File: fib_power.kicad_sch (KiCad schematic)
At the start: 0 parts

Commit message: added several ICs, implementted schematics for charger, boost converter and LDOs
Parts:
- added C21, C28, C29, C31, C32: 10uF, symbol Device:C_Small
- added C22, C23, C25, C26, C27: 22uF, symbol Device:C_Small
- added C24: 330uF, symbol Device:C_Polarized_Small
- added C30, C33: 0.1uF, symbol Device:C_Small
- added L2: 1uH, symbol Device:L_Small
- added R11, R12: 100K, symbol Device:R_Small
- added U2: TPS61022RWUR, Fibel2:TPS61022RWUR, symbol Fibel2:TPS61022RWUR
- added U5: TLV75718PDBV, Package_TO_SOT_SMD:SOT-23-5, symbol Regulator_Linear:TLV75718PDBV
- added U6: TLV75733PDBV, Package_TO_SOT_SMD:SOT-23-5, symbol Regulator_Linear:TLV75733PDBV
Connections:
- new net: L2.2, U2.2 (SW)
- new net: R12.1, U2.4 (FB)
- new net: C22.2, C23.2, C24.2, C25.2
- new net +1V8: C28.1, C29.1, C30.1, U5.5 (OUT)
- new net +3V3: C31.1, C32.1, C33.1, U6.5 (OUT)
- new net +5V: C22.1, C23.1, C24.1, C25.1, C26.1, C27.1, R11.2, R12.2, U2.3 (VOUT), U5.1 (IN), U6.1 (IN)
- new net 5V_EN: U2.5 (EN)
- new net CARRIER_EN: U5.3 (EN), U6.3 (EN)
- new net GND: C21.2, C26.2, C27.2, C28.2, C29.2, C30.2, C31.2, C32.2, C33.2, R11.1, U2.1 (GND), U5.2 (GND), U6.2 (GND)
- new net VCC: C21.1, L2.1, U2.6 (MODE), U2.7 (VIN)
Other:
- note added: "RTC"
- note added: "SEQUENCING"

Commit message: added symbol&footprint for orin/sodimm, added a bunch of specs and docs, partially implemented audio, full steam ahead
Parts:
- C21, C28, C29, C30, C31, C32, C33: footprint (none) -> Capacitor_SMD:C_0603_1608Metric
- C22, C23, C25, C26, C27: footprint (none) -> Capacitor_SMD:C_0805_2012Metric
- C24: footprint (none) -> Capacitor_Tantalum_SMD:CP_EIA-6032-15_Kemet-U
- R11, R12: footprint (none) -> Resistor_SMD:R_0603_1608Metric

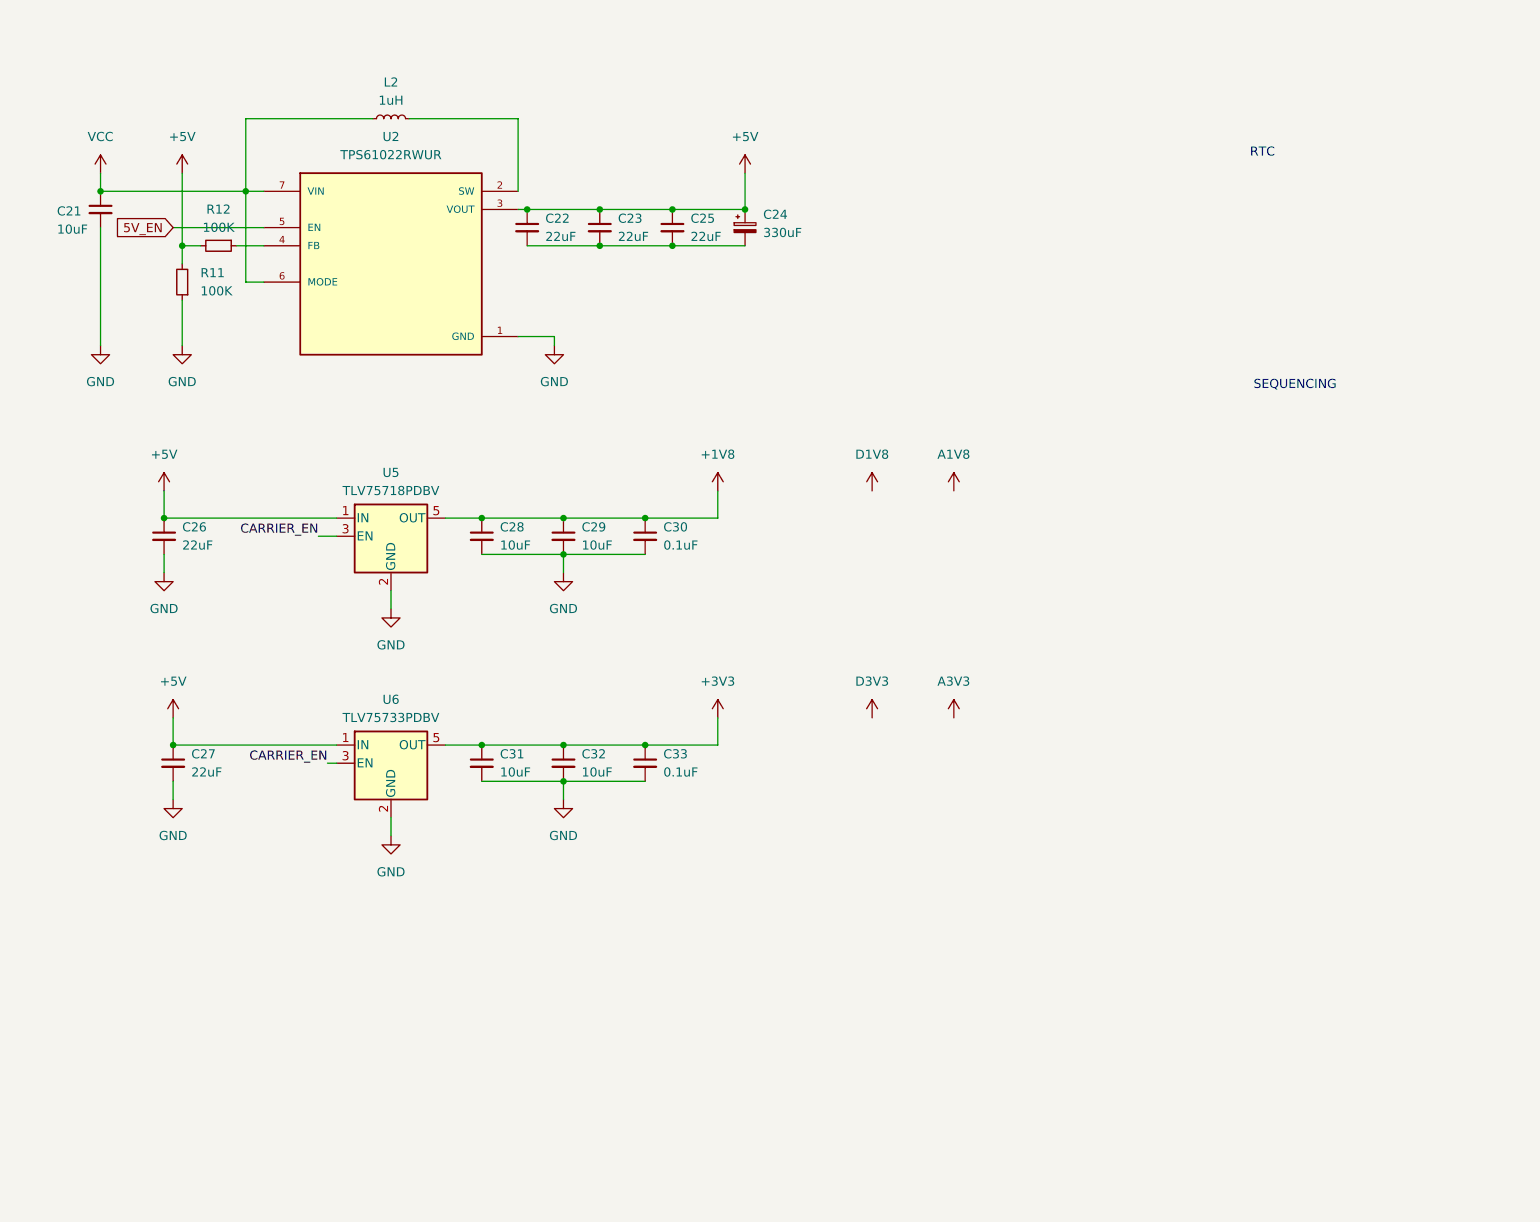
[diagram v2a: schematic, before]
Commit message: added usb+PD+DP & pcie implementations from antmicro design, added specs for USB components, rethought power+usb arch
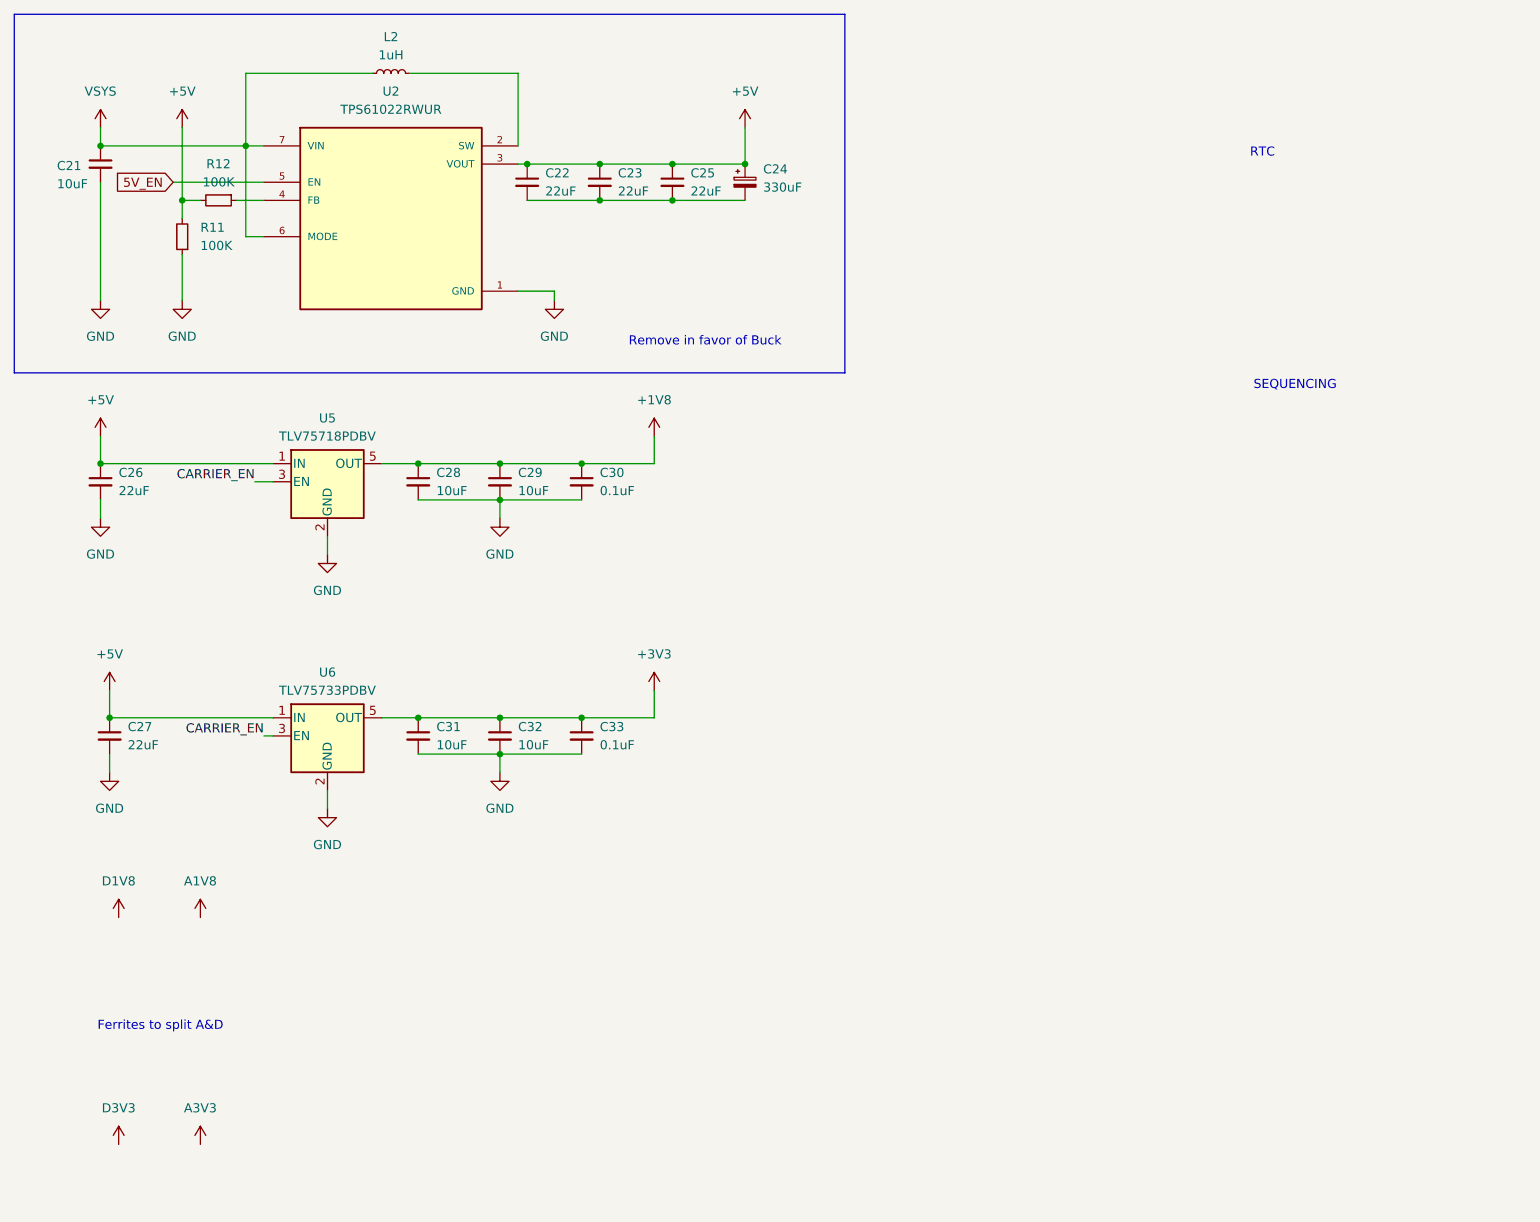
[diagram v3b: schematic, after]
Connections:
- net VCC renamed VSYS
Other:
- note added: "Ferrites to split A&D"
- note added: "Remove in favor of Buck"
- moved on the sheet: C21, C22, C23, C24, C25, C26, C27, C28, C29, C30, C31, C32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

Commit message: added nets for 40 pin headers (epd & rpi header) connected some of the nets i'm reeusing
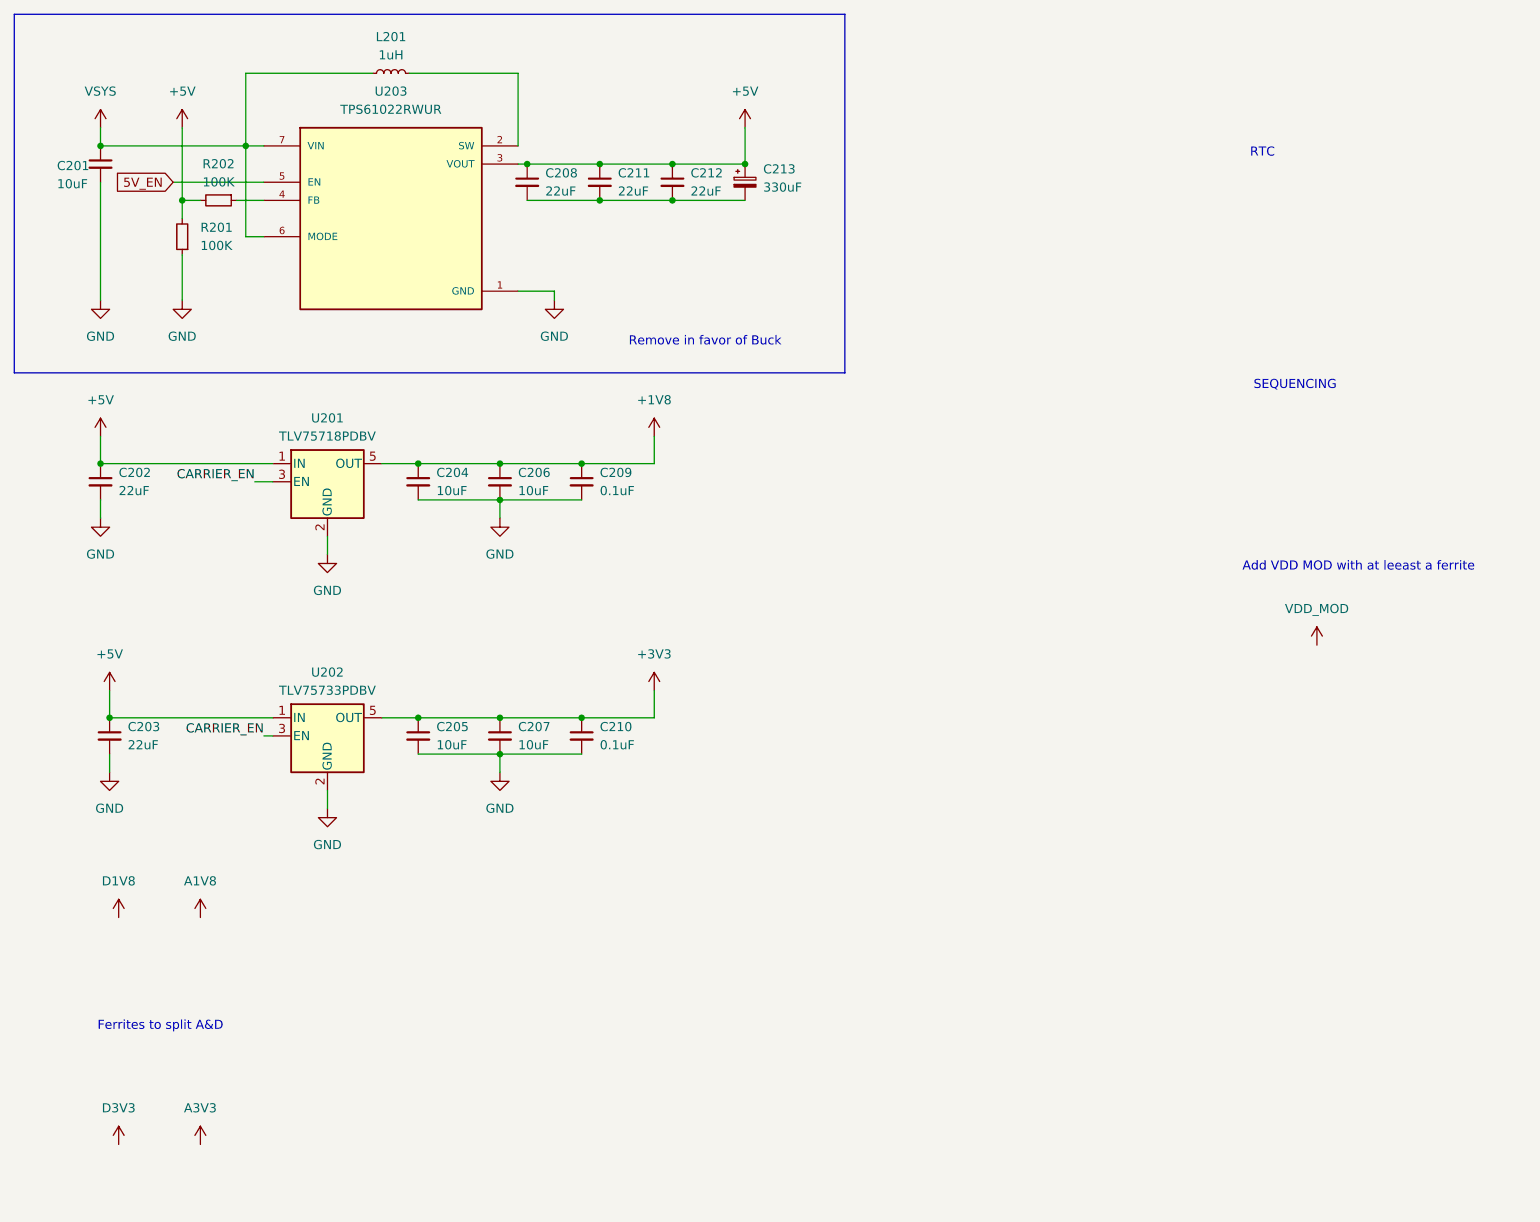
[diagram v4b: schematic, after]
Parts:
- renumbered C21 to C201, C26 to C202, C27 to C203, C28 to C204, C31 to C205, C29 to C206, C32 to C207, C22 to C208, C30 to C209, C33 to C210, C23 to C211, C25 to C212, C24 to C213, L2 to L201, R11 to R201, R12 to R202, U5 to U201, U6 to U202, U2 to U203
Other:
- note added: "Add VDD MOD with at leeast a ferrite"

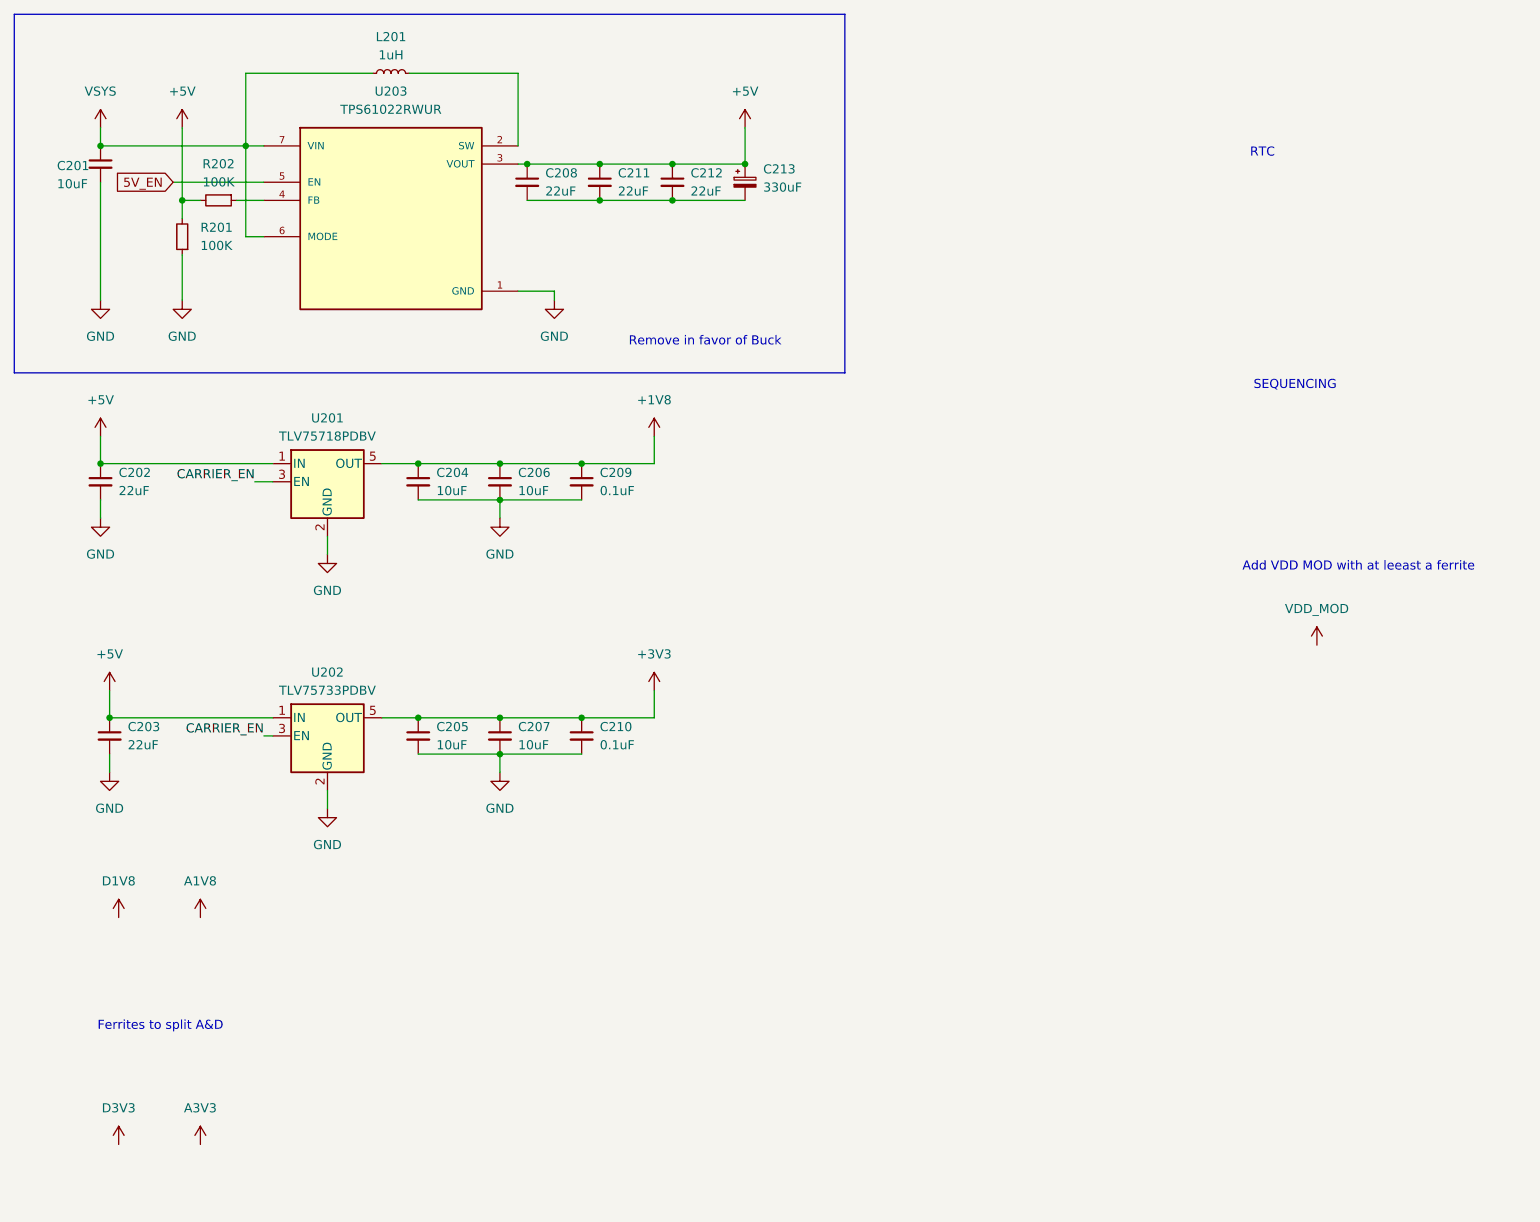
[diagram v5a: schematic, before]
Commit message: added buck converter, refactoored peripherals and updated gpio/SPI/i2c mapping
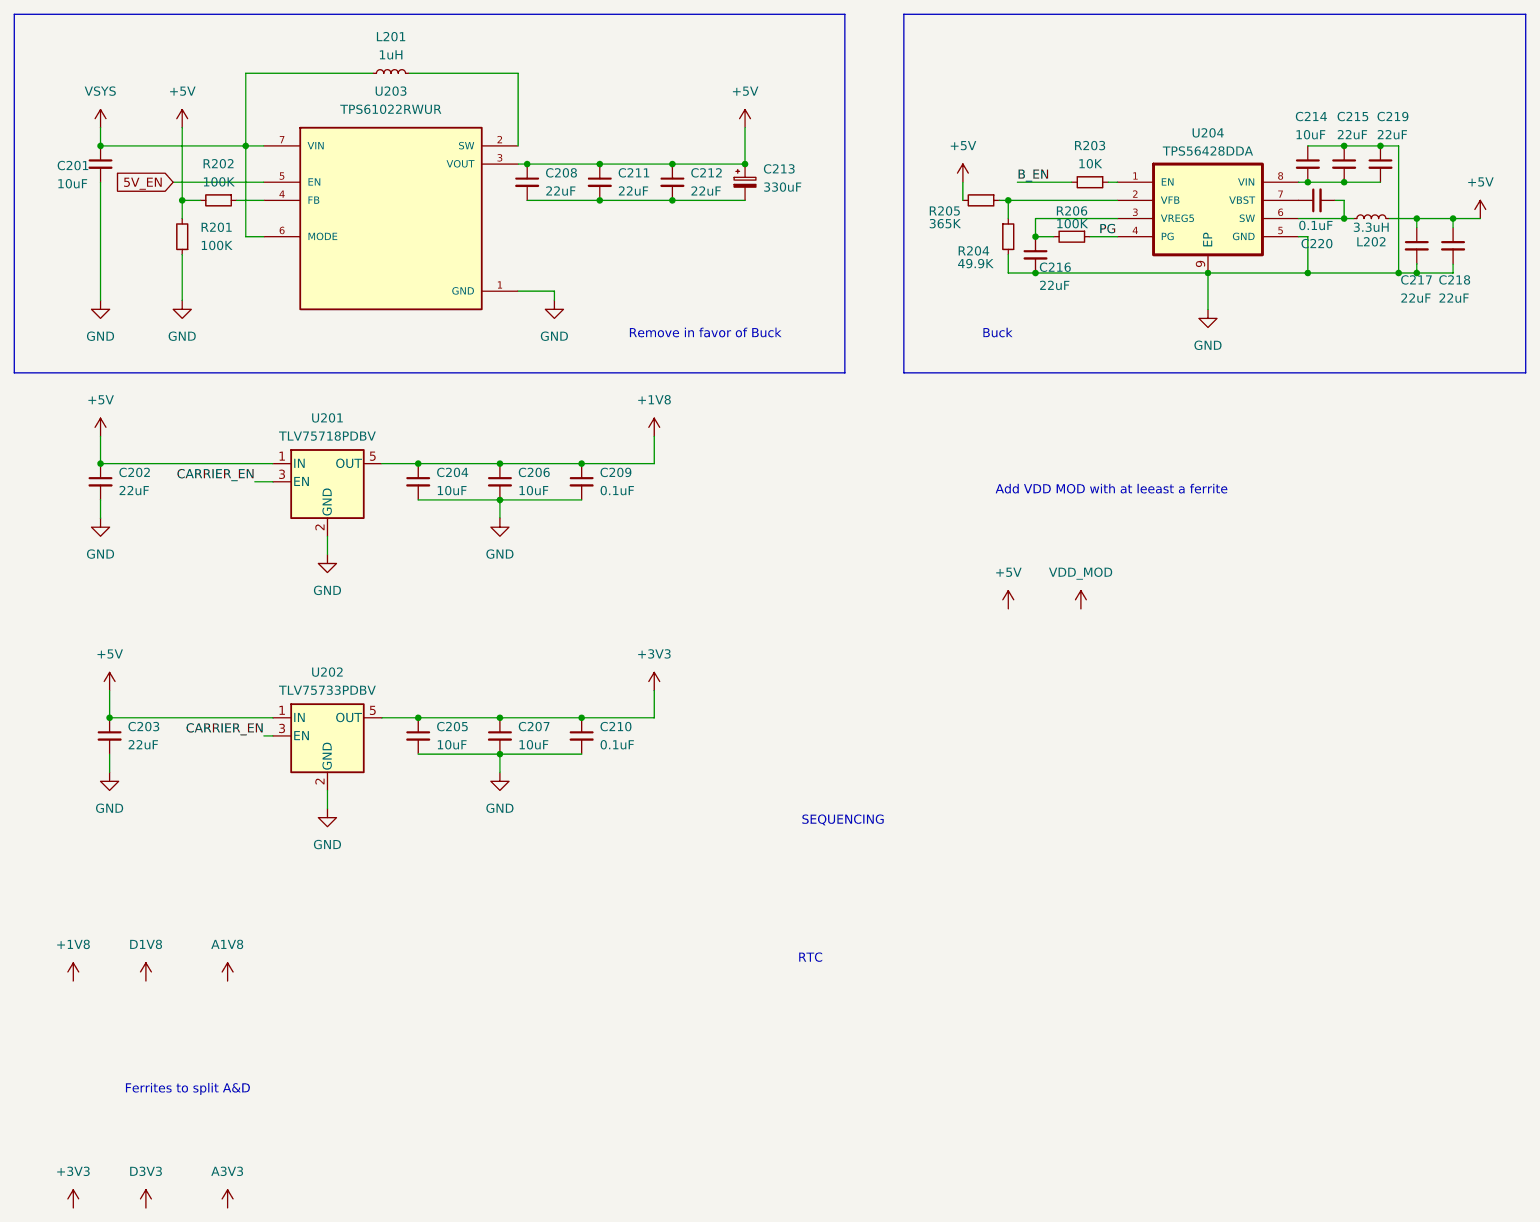
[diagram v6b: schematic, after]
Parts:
- added C214: 10uF, Capacitor_SMD:C_0603_1608Metric, symbol Device:C_Small
- added C215, C216, C218, C219: 22uF, Capacitor_SMD:C_0805_2012Metric, symbol Device:C_Small
- added C217: 22uF, Capacitor_SMD:C_0603_1608Metric, symbol Device:C_Small
- added C220: 0.1uF, Capacitor_SMD:C_0805_2012Metric, symbol Device:C_Small
- added L202: 3.3uH, symbol Device:L_Small
- added R203: 10K, Resistor_SMD:R_0603_1608Metric, symbol Device:R_Small
- added R204: 49.9K, Resistor_SMD:R_0603_1608Metric, symbol Device:R_Small
- added R205: 365K, Resistor_SMD:R_0603_1608Metric, symbol Device:R_Small
- added R206: 100K, Resistor_SMD:R_0603_1608Metric, symbol Device:R_Small
- added U204: TPS56428DDA, Fibel2:TPS56428DDA, symbol Fibel2:TPS56428DDA
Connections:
- net +5V: now also C217.1, C218.1, L202.2, R205.2
- net GND: now also C214.1, C215.1, C216.2, C217.2, C218.2, C219.1, R204.2, U204.5 (GND), U204.9 (EP)
- new net: C214.2, C215.2, C219.2, U204.8 (VIN)
- new net: C216.1, R206.2, U204.3 (VREG5)
- new net: R204.1, R205.1, U204.2 (VFB)
- new net: C220.2, L202.1, U204.6 (SW)
- new net: R203.1, U204.1 (EN)
- new net: C220.1, U204.7 (VBST)
- new net B_EN: R203.2
- new net PG: R206.1, U204.4 (PG)
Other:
- note added: "Buck"
